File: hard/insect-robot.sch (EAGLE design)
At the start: 13 parts, among them Q1 AO3400, SW1 SWITCH-DT, U1 ATMEGA328P-QFN32, U2 PW0316

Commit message: Redesign
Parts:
- removed Q1: AO3400, MyLibrary:MOSFET-SOT23
- removed R3: 1kΩ, MyLibrary:RES-0603
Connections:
- removed net BAT-COM: BAT1.+, SW1.COM
- removed net SWITCH-B: Q1.D, SW1.B
- new net RST: HD2.5, U1.PC6(RESET)
- new net VDD: D1.+, SW1.A, U1.AVCC, U1.VCC@1, U1.VCC@2, U2.VCC3.3
- net GND: no longer R3.2
- net L: now also HD1.1, U1.PC1(ADC1); no longer HD1.3, U1.PC0(ADC0)
- net R: now also HD1.3, U1.PC0(ADC0); no longer HD1.1, Q1.G, Q1.S, R3.1, U1.PC1(ADC1)
- net VBAT: now also BAT1.+, SW1.COM; no longer D1.+, SW1.A, U1.AVCC, U1.VCC@1, U1.VCC@2, U2.VCC3.3
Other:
- note removed: "Powered off & connected to charger -> MOSFET breaks over and begins to be charged."
- moved on the sheet: BAT1, SW1

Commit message: Redesign finished
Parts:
- D1: value LED-RGB-A-3528 -> LED-RGB-A-0603; device MyLibrary:LED-RGB-A-3528 -> MyLibrary:LED-RGB-A-0603
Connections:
- net B-: now also RP1D.1; no longer RP1B.1
- net R-: now also RP1B.1; no longer RP1D.1
- net RB-: now also RP1D.2; no longer RP1B.2
- net RR-: now also RP1B.2; no longer RP1D.2
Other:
- moved on the sheet: RP1B, RP1D
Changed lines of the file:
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@@
 <part name="R2" library="MyLibrary" deviceset="RES" device="-0603" value="1kΩ"/>
 <part name="SUPPLY25" library="MyLibrary" deviceset="GND" device=""/>
-<part name="D1" library="MyLibrary" deviceset="LED-RGB-A" device="-3528"/>
+<part name="D1" library="MyLibrary" deviceset="LED-RGB-A" device="-0603" value="LED-RGB-A-0603"/>
 <part name="SUPPLY8" library="MyLibrary" deviceset="VDD" device=""/>
 <part name="C1" library="MyLibrary" deviceset="CAP" device="-0603" value="100nF"/>
@@
 <attribute name="VALUE" x="71.12" y="-22.86" size="1.778" layer="96"/>
 </instance>
-<instance part="RP1" gate="B" x="40.64" y="-10.16" smashed="yes">
-<attribute name="NAME" x="43.18" y="-10.16" size="1.778" layer="95"/>
-<attribute name="VALUE" x="50.8" y="-10.16" size="1.778" layer="96"/>
+<instance part="RP1" gate="B" x="40.64" y="-5.08" smashed="yes">
+<attribute name="NAME" x="43.18" y="-5.08" size="1.778" layer="95"/>
+<attribute name="VALUE" x="50.8" y="-5.08" size="1.778" layer="96"/>
 </instance>
 <instance part="RP1" gate="C" x="40.64" y="-7.62" smashed="yes">
@@
 <attribute name="VALUE" x="50.8" y="-7.62" size="1.778" layer="96"/>
 </instance>
-<instance part="RP1" gate="D" x="40.64" y="-5.08" smashed="yes">
-<attribute name="NAME" x="43.18" y="-5.08" size="1.778" layer="95"/>
-<attribute name="VALUE" x="50.8" y="-5.08" size="1.778" layer="96"/>
+<instance part="RP1" gate="D" x="40.64" y="-10.16" smashed="yes">
+<attribute name="NAME" x="43.18" y="-10.16" size="1.778" layer="95"/>
+<attribute name="VALUE" x="50.8" y="-10.16" size="1.778" layer="96"/>
 </instance>
 <instance part="SUPPLY11" gate="GND" x="-86.36" y="35.56"/>
@@
 <segment>
 <pinref part="U1" gate="P" pin="PB0(ICP1)"/>
-<pinref part="RP1" gate="D" pin="2"/>
+<pinref part="RP1" gate="B" pin="2"/>
 </segment>
 </net>
@@
 <segment>
 <pinref part="U1" gate="P" pin="PB2(SS/OC1B)"/>
-<pinref part="RP1" gate="B" pin="2"/>
+<pinref part="RP1" gate="D" pin="2"/>
 </segment>
 </net>
@@
 <segment>
 <pinref part="D1" gate="A" pin="R-"/>
+<wire x1="55.88" y1="-5.08" x2="45.72" y2="-5.08" width="0.1524" layer="91"/>
+<pinref part="RP1" gate="B" pin="1"/>
+</segment>
+</net>
+<net name="G-" class="0">
+<segment>
+<pinref part="D1" gate="A" pin="G-"/>
+<wire x1="55.88" y1="-7.62" x2="45.72" y2="-7.62" width="0.1524" layer="91"/>
+<pinref part="RP1" gate="C" pin="1"/>
+</segment>
+</net>
+<net name="B-" class="0">
+<segment>
+<pinref part="D1" gate="A" pin="B-"/>
+<wire x1="55.88" y1="-10.16" x2="45.72" y2="-10.16" width="0.1524" layer="91"/>
 <pinref part="RP1" gate="D" pin="1"/>
-<wire x1="45.72" y1="-5.08" x2="55.88" y2="-5.08" width="0.1524" layer="91"/>
-</segment>
-</net>
-<net name="G-" class="0">
-<segment>
-<pinref part="D1" gate="A" pin="G-"/>
-<pinref part="RP1" gate="C" pin="1"/>
-<wire x1="45.72" y1="-7.62" x2="55.88" y2="-7.62" width="0.1524" layer="91"/>
-</segment>
-</net>
-<net name="B-" class="0">
-<segment>
-<pinref part="D1" gate="A" pin="B-"/>
-<pinref part="RP1" gate="B" pin="1"/>
-<wire x1="45.72" y1="-10.16" x2="55.88" y2="-10.16" width="0.1524" layer="91"/>
-</segment>
-</net>
+</segment>
+</net>

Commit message: PWM pins
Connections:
- removed net MOSI: HD2.4, U1.PB3(MOSI)
- removed net RB-: RP1D.2, U1.PB2(SS/OC1B)
- new net RB-/MOSI: HD2.4, RP1D.2, U1.PB3(MOSI/OC2A)
- net L: now also U1.PB2(SS/OC1B)
- net LINK: now also U1.PD3(INT1/OC2B); no longer U1.PD3(INT1)
- net R: now also U1.PB1(OC1A)
- net RG-: now also U1.PD6(AIN0/OC0A); no longer U1.PB1(OC1A)
- net RR-: now also U1.PD5(T1/OC0B); no longer U1.PB0(ICP1)
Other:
- moved on the sheet: D1, RP1B, RP1C, RP1D
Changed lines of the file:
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@@
 </instance>
 <instance part="SUPPLY25" gate="GND" x="134.62" y="-27.94" rot="R90"/>
-<instance part="D1" gate="A" x="66.04" y="-7.62" rot="MR270"/>
-<instance part="SUPPLY8" gate="G$1" x="78.74" y="-7.62" rot="R270"/>
+<instance part="D1" gate="A" x="81.28" y="-10.16" rot="MR270"/>
+<instance part="SUPPLY8" gate="G$1" x="93.98" y="-10.16" rot="R270"/>
 <instance part="C1" gate="A" x="-35.56" y="2.54" rot="R90"/>
 <instance part="SUPPLY10" gate="GND" x="-43.18" y="2.54" rot="R270"/>
@@
 <attribute name="VALUE" x="71.12" y="-22.86" size="1.778" layer="96"/>
 </instance>
-<instance part="RP1" gate="B" x="40.64" y="-5.08" smashed="yes">
-<attribute name="NAME" x="43.18" y="-5.08" size="1.778" layer="95"/>
-<attribute name="VALUE" x="50.8" y="-5.08" size="1.778" layer="96"/>
-</instance>
-<instance part="RP1" gate="C" x="40.64" y="-7.62" smashed="yes">
-<attribute name="NAME" x="43.18" y="-7.62" size="1.778" layer="95"/>
-<attribute name="VALUE" x="50.8" y="-7.62" size="1.778" layer="96"/>
-</instance>
-<instance part="RP1" gate="D" x="40.64" y="-10.16" smashed="yes">
-<attribute name="NAME" x="43.18" y="-10.16" size="1.778" layer="95"/>
-<attribute name="VALUE" x="50.8" y="-10.16" size="1.778" layer="96"/>
+<instance part="RP1" gate="B" x="55.88" y="-7.62" smashed="yes">
+<attribute name="NAME" x="58.42" y="-7.62" size="1.778" layer="95"/>
+<attribute name="VALUE" x="66.04" y="-7.62" size="1.778" layer="96"/>
+</instance>
+<instance part="RP1" gate="C" x="55.88" y="-10.16" smashed="yes">
+<attribute name="NAME" x="58.42" y="-10.16" size="1.778" layer="95"/>
+<attribute name="VALUE" x="66.04" y="-10.16" size="1.778" layer="96"/>
+</instance>
+<instance part="RP1" gate="D" x="55.88" y="-12.7" smashed="yes">
+<attribute name="NAME" x="58.42" y="-12.7" size="1.778" layer="95"/>
+<attribute name="VALUE" x="66.04" y="-12.7" size="1.778" layer="96"/>
 </instance>
 <instance part="SUPPLY11" gate="GND" x="-86.36" y="35.56"/>
@@
 <label x="-38.1" y="-7.62" size="1.778" layer="95" font="vector" rot="R180"/>
 </segment>
+<segment>
+<pinref part="U1" gate="P" pin="PB2(SS/OC1B)"/>
+<wire x1="35.56" y1="-10.16" x2="40.64" y2="-10.16" width="0.1524" layer="91"/>
+<label x="40.64" y="-10.16" size="1.778" layer="95" font="vector"/>
+</segment>
 </net>
 <net name="R" class="0">
@@
 <label x="-38.1" y="-5.08" size="1.778" layer="95" font="vector" rot="R180"/>
 </segment>
+<segment>
+<pinref part="U1" gate="P" pin="PB1(OC1A)"/>
+<wire x1="35.56" y1="-7.62" x2="40.64" y2="-7.62" width="0.1524" layer="91"/>
+<label x="40.64" y="-7.62" size="1.778" layer="95" font="vector"/>
+</segment>
 </net>
 <net name="RXD" class="0">
@@
 </segment>
 <segment>
-<pinref part="U1" gate="P" pin="PD3(INT1)"/>
+<pinref part="U1" gate="P" pin="PD3(INT1/OC2B)"/>
 <wire x1="35.56" y1="12.7" x2="40.64" y2="12.7" width="0.1524" layer="91"/>
 <label x="40.64" y="12.7" size="1.778" layer="95" font="vector"/>
 </segment>
 </net>
-<net name="MOSI" class="0">
-<segment>
-<pinref part="U1" gate="P" pin="PB3(MOSI)"/>
-<wire x1="35.56" y1="-12.7" x2="45.72" y2="-12.7" width="0.1524" layer="91"/>
-<label x="45.72" y="-12.7" size="1.778" layer="95" font="vector"/>
+<net name="RB-/MOSI" class="0">
+<segment>
+<pinref part="U1" gate="P" pin="PB3(MOSI/OC2A)"/>
+<label x="38.1" y="-12.7" size="1.778" layer="95" font="vector"/>
+<pinref part="RP1" gate="D" pin="2"/>
+<wire x1="50.8" y1="-12.7" x2="35.56" y2="-12.7" width="0.1524" layer="91"/>
 </segment>
 <segment>
@@
 </segment>
 </net>
-<net name="RR-" class="0">
-<segment>
-<pinref part="U1" gate="P" pin="PB0(ICP1)"/>
-<pinref part="RP1" gate="B" pin="2"/>
-</segment>
-</net>
-<net name="RG-" class="0">
-<segment>
-<pinref part="U1" gate="P" pin="PB1(OC1A)"/>
-<pinref part="RP1" gate="C" pin="2"/>
-</segment>
-</net>
-<net name="RB-" class="0">
-<segment>
-<pinref part="U1" gate="P" pin="PB2(SS/OC1B)"/>
-<pinref part="RP1" gate="D" pin="2"/>
-</segment>
-</net>
 <net name="R-" class="0">
 <segment>
 <pinref part="D1" gate="A" pin="R-"/>
-<wire x1="55.88" y1="-5.08" x2="45.72" y2="-5.08" width="0.1524" layer="91"/>
+<wire x1="71.12" y1="-7.62" x2="60.96" y2="-7.62" width="0.1524" layer="91"/>
 <pinref part="RP1" gate="B" pin="1"/>
 </segment>
@@
 <segment>
 <pinref part="D1" gate="A" pin="G-"/>
-<wire x1="55.88" y1="-7.62" x2="45.72" y2="-7.62" width="0.1524" layer="91"/>
+<wire x1="71.12" y1="-10.16" x2="60.96" y2="-10.16" width="0.1524" layer="91"/>
 <pinref part="RP1" gate="C" pin="1"/>
 </segment>
@@
 <segment>
 <pinref part="D1" gate="A" pin="B-"/>
-<wire x1="55.88" y1="-10.16" x2="45.72" y2="-10.16" width="0.1524" layer="91"/>
+<wire x1="71.12" y1="-12.7" x2="60.96" y2="-12.7" width="0.1524" layer="91"/>
 <pinref part="RP1" gate="D" pin="1"/>
 </segment>
@@
 </segment>
 </net>
+<net name="RR-" class="0">
+<segment>
+<pinref part="RP1" gate="B" pin="2"/>
+<pinref part="U1" gate="P" pin="PD5(T1/OC0B)"/>
+<wire x1="35.56" y1="7.62" x2="50.8" y2="7.62" width="0.1524" layer="91"/>
+<wire x1="50.8" y1="7.62" x2="50.8" y2="-7.62" width="0.1524" layer="91"/>
+</segment>
+</net>
+<net name="RG-" class="0">
+<segment>
+<pinref part="RP1" gate="C" pin="2"/>
+<wire x1="50.8" y1="-10.16" x2="48.26" y2="-10.16" width="0.1524" layer="91"/>
+<wire x1="48.26" y1="-10.16" x2="48.26" y2="5.08" width="0.1524" layer="91"/>
+<pinref part="U1" gate="P" pin="PD6(AIN0/OC0A)"/>
+<wire x1="48.26" y1="5.08" x2="35.56" y2="5.08" width="0.1524" layer="91"/>
+</segment>
+</net>

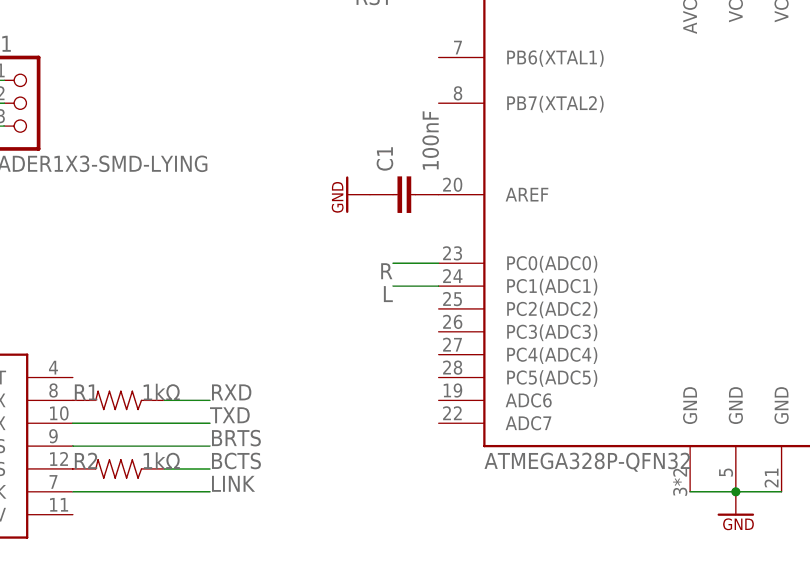
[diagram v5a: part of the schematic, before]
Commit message: Remove non-PWM elctrode pins
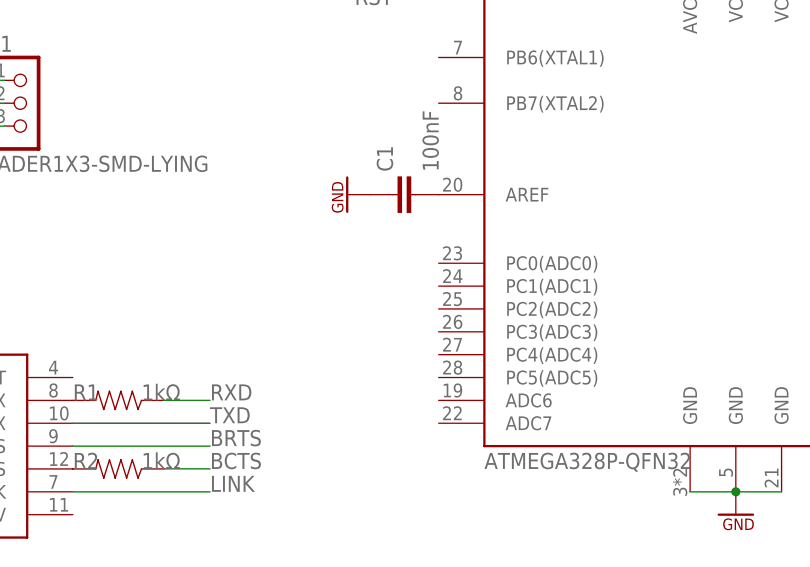
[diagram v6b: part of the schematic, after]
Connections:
- net L: no longer U1.PC1(ADC1)
- net R: no longer U1.PC0(ADC0)
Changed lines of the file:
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@@
-</segment>
-<segment>
-<pinref part="U1" gate="P" pin="PC1(ADC1)"/>
-<wire x1="-33.02" y1="-7.62" x2="-38.1" y2="-7.62" width="0.1524" layer="91"/>
-<label x="-38.1" y="-7.62" size="1.778" layer="95" font="vector" rot="R180"/>
 </segment>
 <segment>
@@
 </segment>
 <segment>
-<pinref part="U1" gate="P" pin="PC0(ADC0)"/>
-<wire x1="-33.02" y1="-5.08" x2="-38.1" y2="-5.08" width="0.1524" layer="91"/>
-<label x="-38.1" y="-5.08" size="1.778" layer="95" font="vector" rot="R180"/>
-</segment>
-<segment>
